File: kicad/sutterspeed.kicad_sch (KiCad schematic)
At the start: 15 parts, among them J1 USB4500, J2 STDC10, SW2 MK-23D33-G4, U1 STM32C071G8Ux, U2 TPS7A20U33, U3 USBLC6-2P6, U4 TLV9061xDPW

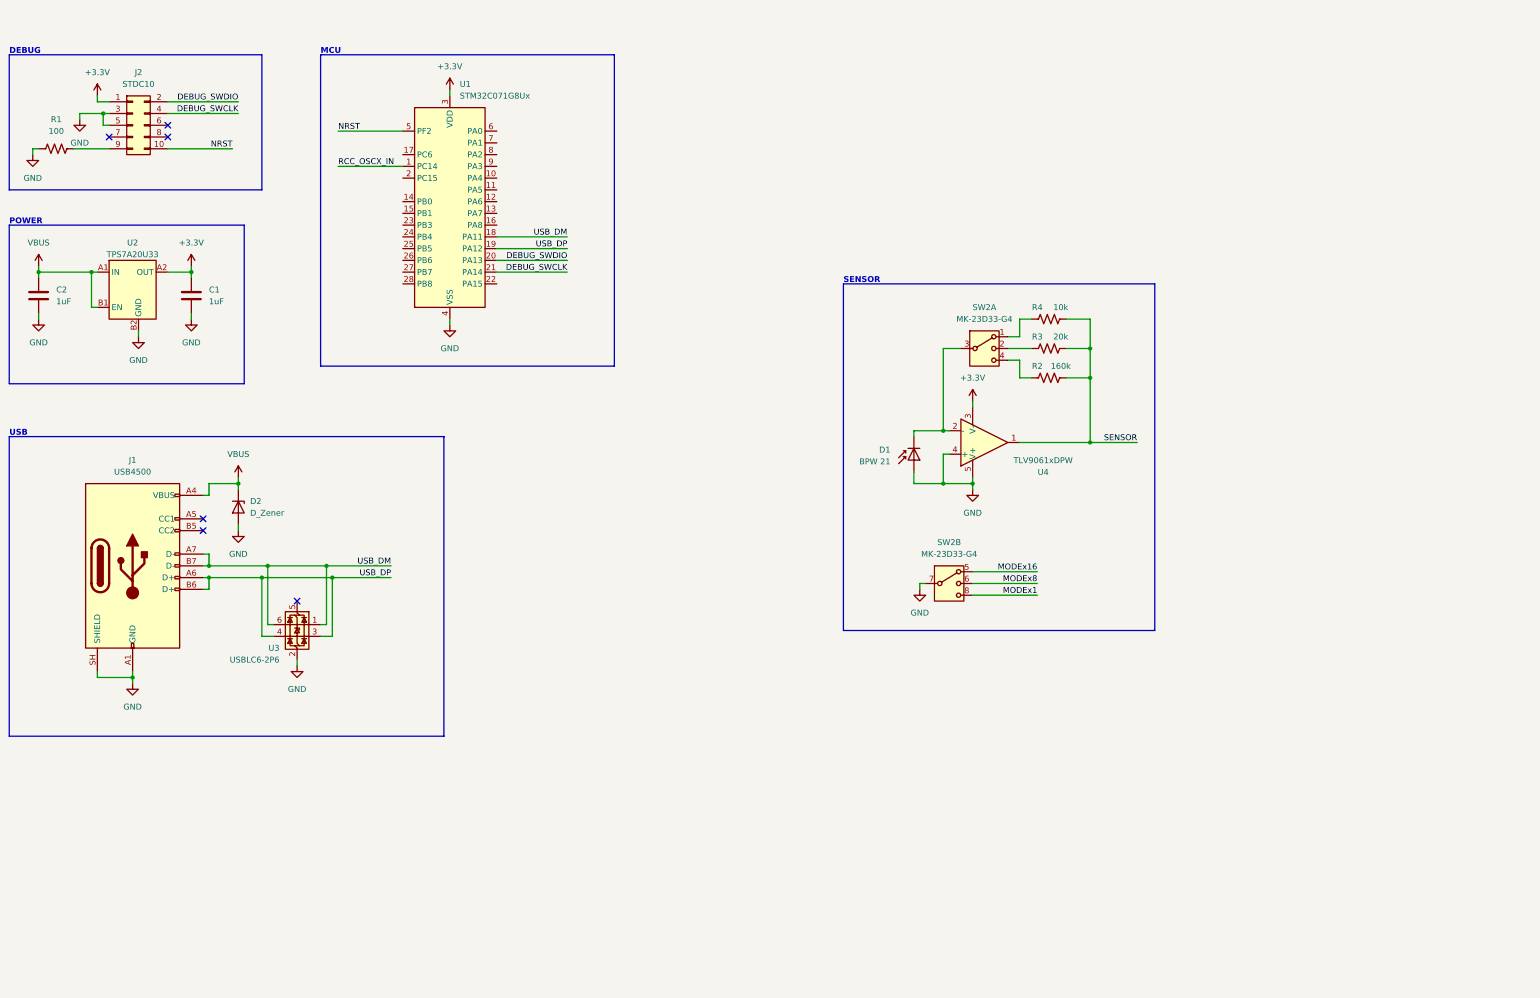
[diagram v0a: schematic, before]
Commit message: Light oscilloscope firmware, Windows viewer and repository clean-up
- firmware 0.3.2: 400 kS/s scope engine (decimation, trigger, roll, shutter pulse capture), USB CDC protocol, DFU entry
- viewer (Rust/egui): scope controls, filters, measurements, cursors, shutter measurement, USB firmware update
- host test of the scope engine
- libraries as submodules; KiCad backups and local state ignored; READMEs

Co-Authored-By: Claude Opus 5.5 <noreply@anthropic.com>
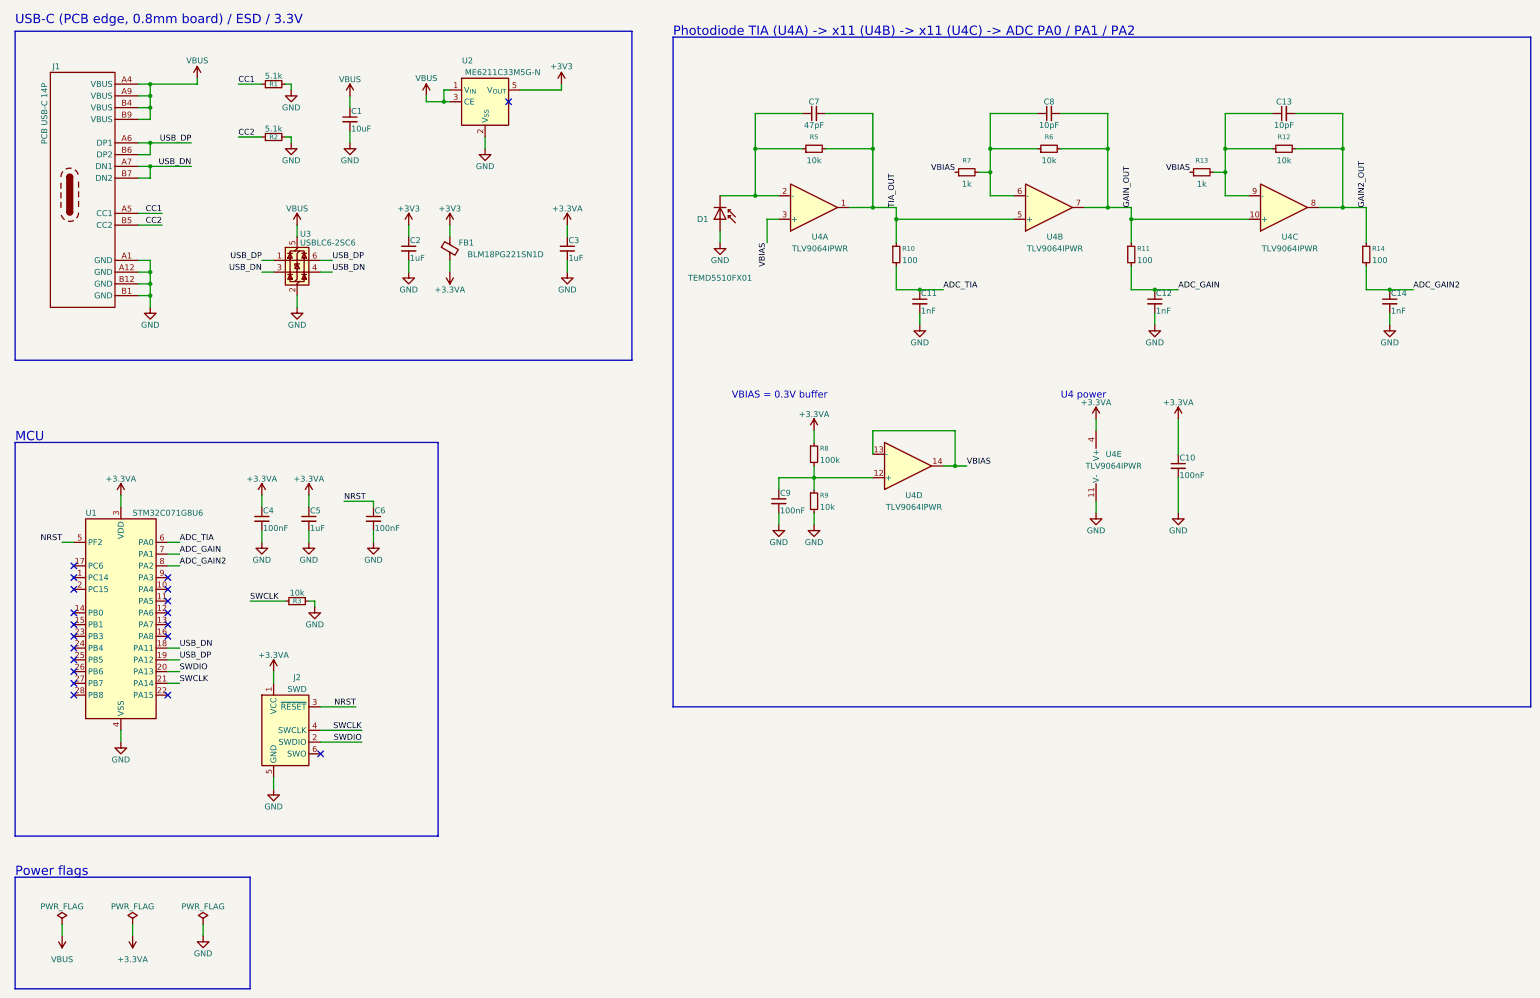
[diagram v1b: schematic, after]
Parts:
- removed C1, C2: 1uF, Capacitor_SMD:C_0402_1005Metric, symbol Device:C
- removed D2: D_Zener, symbol Device:D_Zener
- removed J1: USB4500, symbol Connector:USB_C_Receptacle_USB2.0_14P
- removed J2: STDC10, Connector_PinHeader_1.27mm:PinHeader_2x07_P1.27mm_Vertical, symbol Connector_Generic:Conn_02x05_Odd_Even
- removed R1: 100, Resistor_SMD:R_0402_1005Metric, symbol Device:R_US
- removed R2: 160k, Resistor_SMD:R_0402_1005Metric, symbol Device:R_US
- removed R3: 20k, Resistor_SMD:R_0402_1005Metric, symbol Device:R_US
- removed R4: 10k, Resistor_SMD:R_0402_1005Metric, symbol Device:R_US
- removed SW2: MK-23D33-G4, Sutterspeed:MK-23D33, symbol Switch:SW_DP3T
- removed U2: TPS7A20U33, symbol Sutterspeed:TPS7A20U33
- removed U3: USBLC6-2P6, Package_TO_SOT_SMD:SOT-666, symbol Power_Protection:USBLC6-2P6
- removed U4: TLV9061xDPW, Package_SON:Texas_X2SON-5_0.8x0.8mm_P0.48mm, symbol Amplifier_Operational:TLV9061xDPW
- added C1: 10uF, Capacitor_SMD:C_0603_1608Metric, symbol Device:C_Small
- added C10, C4, C6, C9: 100nF, Capacitor_SMD:C_0402_1005Metric, symbol Device:C_Small
- added C11, C12, C14: 1nF, Capacitor_SMD:C_0402_1005Metric, symbol Device:C_Small
- added C13, C8: 10pF, Capacitor_SMD:C_0402_1005Metric, symbol Device:C_Small
- added C2, C3, C5: 1uF, Capacitor_SMD:C_0402_1005Metric, symbol Device:C_Small
- added C7: 47pF, Capacitor_SMD:C_0402_1005Metric, symbol Device:C_Small
- added FB1: BLM18PG221SN1D, Inductor_SMD:L_0603_1608Metric, symbol Device:FerriteBead_Small
- added J1: PCB USB-C 14P, PCB_USBC:PCBTypeC_14P, symbol PCB_USBC:PCBTypeC_14P
- added J2: SWD, Connector:Tag-Connect_TC2030-IDC-NL_2x03_P1.27mm_Vertical, symbol Connector:Conn_ARM_SWD_TagConnect_TC2030-NL
- added R1, R2: 5.1k, Resistor_SMD:R_0402_1005Metric, symbol Device:R_Small
- added R10, R11, R14: 100, Resistor_SMD:R_0402_1005Metric, symbol Device:R_Small
- added R12, R3, R5, R6, R9: 10k, Resistor_SMD:R_0402_1005Metric, symbol Device:R_Small
- added R13, R7: 1k, Resistor_SMD:R_0402_1005Metric, symbol Device:R_Small
- added R8: 100k, Resistor_SMD:R_0402_1005Metric, symbol Device:R_Small
- added U2: ME6211C33M5G-N, Package_TO_SOT_SMD:SOT-23-5, symbol Regulator_Linear:ME6211C33M5
- added U3: USBLC6-2SC6, Package_TO_SOT_SMD:SOT-23-6, symbol Power_Protection:USBLC6-2SC6
- added U4: TLV9064IPWR, Package_SO:TSSOP-14_4.4x5mm_P0.65mm, symbol Amplifier_Operational:TLV9064
- D1: value BPW 21 -> TEMD5510FX01; footprint (none) -> personal:Vishay_TEMD5510FX01; LCSC (none) -> C94856; MPN (none) -> TEMD5510FX01
- U1: value STM32C071G8Ux -> STM32C071G8U6; LCSC (none) -> C44521811
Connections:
- net GND: now also C1.2, C10.2, C11.2, C12.2, C14.2, C2.2, C3.2, C4.2, C5.2, C6.2, C9.2, J1.A1 (GND), J1.A12 (GND), J1.B1 (GND), J1.B12 (GND), J2.5 (GND), R1.2, R2.2, R3.2, R9.2, U2.2 (V_{SS}), U3.2 (GND), U4.11 (V-)
- net NRST: now also C6.1, J2.3 (~{RESET})
- net USB_DP: now also J1.A6 (DP1), J1.B6 (DP2), U3.1 (I/O1), U3.6 (I/O1)
- net VBUS: now also C1.1, J1.A4 (VBUS), J1.A9 (VBUS), J1.B4 (VBUS), J1.B9 (VBUS), U2.1 (V_{IN}), U2.3 (CE), U3.5 (VBUS)
- net at D1.1 (K): now also C7.1, R5.1, U4.2 (-)
- net ADC_TIA: now reaches U1.6 (PA0)
- net ADC_TIA: now also C11.1, R10.2
- net ADC_GAIN: now reaches U1.7 (PA1)
- net ADC_GAIN: now also C12.1, R11.2
- net ADC_GAIN2: now reaches U1.8 (PA2)
- net ADC_GAIN2: now also C14.1, R14.2
- net +3.3V renamed +3.3VA
- net +3.3VA: now also C10.1, C3.1, C4.1, C5.1, FB1.2, J2.1 (VCC), R8.1, U4.4 (V+)
- net DEBUG_SWCLK renamed SWCLK
- net SWCLK: now also J2.4 (SWCLK), R3.1
- net DEBUG_SWDIO renamed SWDIO
- net SWDIO: now also J2.2 (SWDIO)
- net RCC_OSCX_IN: no longer names the net of U1.1 (PC14)
- net USB_DM renamed USB_DN
- net USB_DN: now also J1.A7 (DN1), J1.B7 (DN2), U3.3 (I/O2), U3.4 (I/O2)
- new net: C8.1, R6.1, R7.2, U4.6 (-)
- new net: C13.1, R12.1, R13.2, U4.9 (-)
- new net: C9.1, R8.2, R9.1, U4.12 (+)
- new net +3V3: C2.1, FB1.1, U2.5 (V_{OUT})
- new net CC1: J1.A5 (CC1), R1.1
- new net CC2: J1.B5 (CC2), R2.1
- new net GAIN2_OUT: C13.2, R12.2, R14.1, U4.8
- new net GAIN_OUT: C8.2, R11.1, R6.2, U4.10 (+), U4.7
- new net TIA_OUT: C7.2, R10.1, R5.2, U4.1, U4.5 (+)
- new net VBIAS: R13.1, R7.1, U4.13 (-), U4.14, U4.3 (+)
- no-connect marks 6 -> 20
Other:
- note added: "Photodiode TIA (U4A) -> x11 (U4B) -> x11 (U4C) -> ADC PA0 / PA1 / PA2"
- note added: "Power flags"
- note added: "U4 power"
- note added: "USB-C (PCB edge, 0.8mm board) / ESD / 3.3V"
- note added: "VBIAS = 0.3V buffer"
- note removed: "DEBUG"
- note removed: "POWER"
- note removed: "SENSOR"
- note removed: "USB"
- title: (none) -> Sutterspeed - shutter speed tester
